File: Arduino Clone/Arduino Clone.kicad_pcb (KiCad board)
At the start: 2 copper layers, 17 parts, among them J1 Digital pins, J2 ICSP, J3 Serial, J4 I2C, U1 24LC1025, U2 24LC1025, U3 DS1337, U4 ATmega328P-AU, Y1 Crystal 32MHz, Y2 Crystal 16MHz

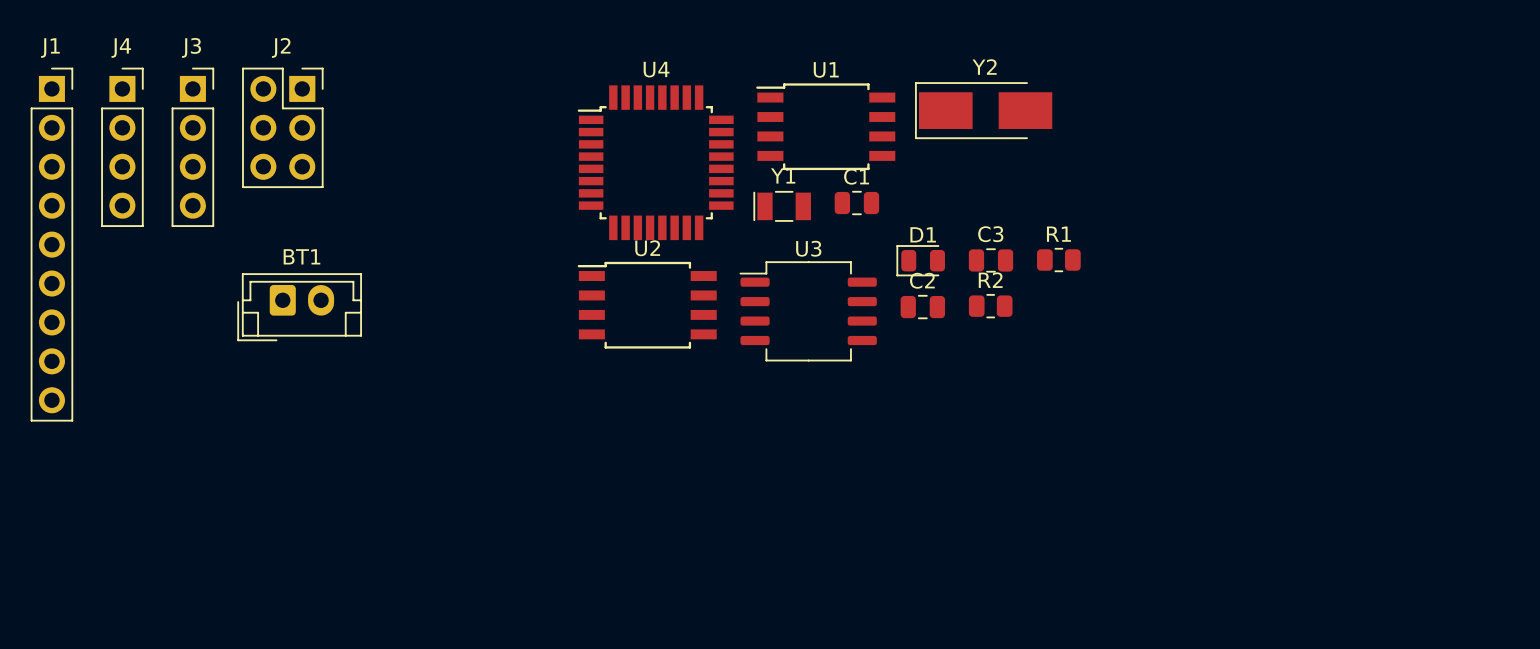
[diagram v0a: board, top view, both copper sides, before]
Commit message: place components
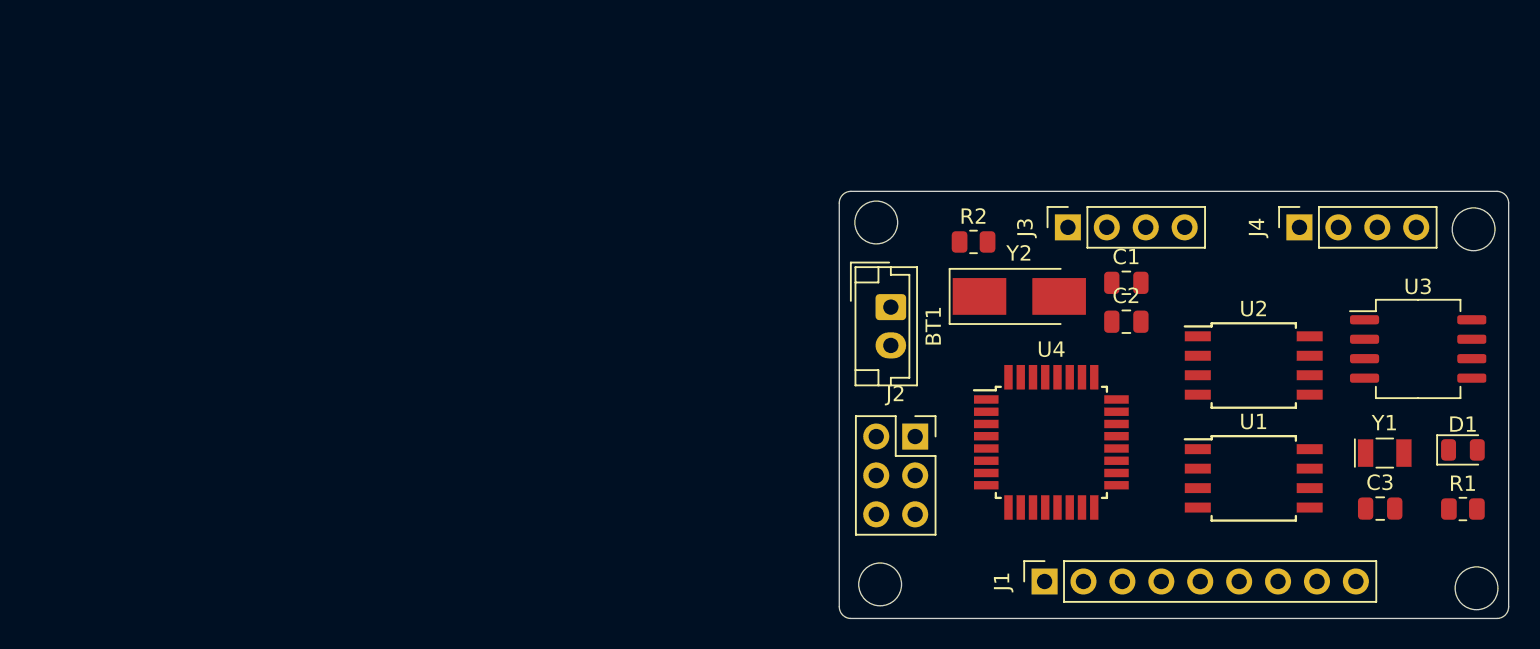
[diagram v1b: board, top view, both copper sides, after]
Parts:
- moved J4 77.4 mm to (172.4, 103.2), turned to 90 degrees
- moved J1 72.3 mm to (155.8, 126.3), turned to 90 degrees
- moved J3 57.8 mm to (157.3, 103.2), turned to 90 degrees
- moved J2 46.0 mm to (147.3, 116.8)
- moved Y1 42.4 mm to (178.0, 117.9)
- moved U3 39.9 mm to (180.1, 111.1)
- moved U2 39.7 mm to (169.4, 112.2)
- moved BT1 39.7 mm to (145.7, 108.4), turned to 270 degrees
- moved D1 37.3 mm to (183.1, 117.7)
- moved U1 36.1 mm to (169.4, 119.6)
- moved U4 31.6 mm to (156.2, 117.2)
- moved R1 31.0 mm to (183.1, 121.6)
- moved C3 30.1 mm to (177.7, 121.5)
- moved C1 18.3 mm to (161.1, 106.8)
- moved C2 13.3 mm to (161.1, 109.3)
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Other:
- board outline added: 43.7 x 27.9 mm

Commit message: main board
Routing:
- net GNDPWR: track 0.00 -> 137.1 mm
- net /Vcc: track 0.00 -> 123.2 mm
- net /SCK: track 0.00 -> 77.5 mm, vias 0 -> 1
- net /SDA: track 0.00 -> 64.4 mm, vias 0 -> 2
- net /RESET: track 0.00 -> 34.3 mm
- net /SCL: track 0.00 -> 29.7 mm
- net Net-(C1-Pad1): track 0.00 -> 26.6 mm, vias 0 -> 2
- net Net-(C2-Pad1): track 0.00 -> 26.0 mm, vias 0 -> 2
- net /D2: track 0.00 -> 21.1 mm, vias 0 -> 1
- net /MOSI: track 0.00 -> 21.0 mm, vias 0 -> 1
- net /Tx: track 0.00 -> 18.9 mm, vias 0 -> 1
- net /ADDS2: track 0.00 -> 18.6 mm, vias 0 -> 2
- net /D8: track 0.00 -> 18.1 mm
- net /ADDS1: track 0.00 -> 17.7 mm, vias 0 -> 2
- net /D4: track 0.00 -> 17.0 mm, vias 0 -> 1
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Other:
- copper layers 2 -> 4

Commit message: final project
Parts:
- added G***: LOGO, logos:Catcuber_10.9x10.9mm, B.Cu at (178.2, 110.3)
- added REF**: KiCad-Logo2_5mm_SilkScreen, Symbol:KiCad-Logo2_5mm_SilkScreen, B.Cu at (164.0, 120.5)
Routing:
- net Net-(C1-Pad1): track 26.6 -> 50.0 mm
- net /SCK: track 77.5 -> 69.4 mm
- net Net-(C2-Pad1): track 26.0 -> 33.1 mm
- net /ADDS1: track 17.7 -> 15.8 mm
- net /Tx: track 18.9 -> 17.0 mm
- net /SDA: track 64.4 -> 66.1 mm
- net GNDPWR: track 137.1 -> 135.7 mm
- net /D4: track 17.0 -> 15.7 mm
- net /ADDS2: track 18.6 -> 17.6 mm
- net /Vcc: track 123.2 -> 122.3 mm
- net /RESET: track 34.3 -> 35.1 mm
- net /D2: track 21.1 -> 21.7 mm
- net /D3: track 16.6 -> 17.1 mm
- added copper zone on B.Cu, net GNDPWR
- added copper zone on F.Cu, net GNDPWR
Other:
- copper layers 4 -> 2
- board text added: "+"
- board text added: "10K"
- board text added: "24LC1025"
- board text added: "Atmega328p"
- board text added: "CATduino Author: Gonzales Loayza Pool Diego v1.0"
- board text added: "D2"
- board text added: "D3"
- board text added: "D4"
- board text added: "D5"
- board text added: "D6"
- board text added: "D7"
- board text added: "D8"
- board text added: "DS1337"
- board text added: "GND"
- board text added: "MISO"
- board text added: "MOSI"
- board text added: "RESET"
- board text added: "Rx"
- board text added: "SCK"
- board text added: "SDA"
- board text added: "Tx"
- board text added: "Vcc"
- board text added: "|"
